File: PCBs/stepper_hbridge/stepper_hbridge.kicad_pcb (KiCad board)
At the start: 2 copper layers, 52.5 x 54.1 mm, 34 parts, among them J1 Conn_02x07_Odd_Even, J2 Conn_02x08_Odd_Even, J3 Conn_02x08_Odd_Even, J4 Conn_01x04_Pin, J5 Conn_01x04_Pin, J6 Conn_01x02_Pin, U1 L298N, U2 L298N, U3 NCP718xSN500

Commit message: both pcbs have smd capacitors, mounting holes, drc errors fixed
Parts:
- added H1: MountingHole, MountingHole:MountingHole_3.2mm_M3, F.Cu at (118.4, 55.7)
- added H2: MountingHole, MountingHole:MountingHole_3.2mm_M3, F.Cu at (162.2, 55.6)
- C2, C4: footprint Capacitor_THT:C_Radial_D8.0mm_H7.0mm_P3.50mm -> Capacitor_SMD:CP_Elec_6.3x7.7
- moved C4 5.44 mm to (119.7, 72.6), turned to 90 degrees
- moved C2 1.32 mm to (160.6, 77.2), turned to 90 degrees
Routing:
- net GND: track 30.9 -> 38.8 mm, vias 6 -> 8
- net +24V: track 172.9 -> 180.1 mm, vias 6 -> 7

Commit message: silkscreen
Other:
- board text added: "A B C D"
- board text added: "D4"
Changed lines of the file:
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@@
 		(tags "capacitor handsolder")
 		(property "Reference" "C6"
-			(at 0 -1.68 0)
+			(at 2.8425 0.17 0)
 			(layer "F.SilkS")
 			(effects
@@
 			(at 8.06 2.12 90)
 			(layer "F.SilkS")
+			(hide yes)
 			(effects
 				(font
@@
 		(tags "capacitor handsolder")
 		(property "Reference" "C9"
-			(at 0 -1.68 90)
+			(at 0.8175 1.82 90)
 			(layer "F.SilkS")
 			(effects
@@
 			(at 0 -4.35 90)
 			(layer "F.SilkS")
+			(hide yes)
 			(effects
 				(font
@@
 			(at 0.399 -1.601 90)
 			(layer "F.SilkS")
+			(hide yes)
 			(effects
 				(font
@@
 			(at 0 -2 90)
 			(layer "F.SilkS")
+			(hide yes)
 			(effects
 				(font
@@
 		(tags "capacitor handsolder")
 		(property "Reference" "C8"
-			(at 0 -1.68 90)
+			(at 1.3275 -1.68 90)
 			(layer "F.SilkS")
 			(effects
@@
 			(at 0 2 180)
 			(layer "B.SilkS")
+			(hide yes)
 			(effects
 				(font
@@
 			(at 0 3.9 0)
 			(layer "B.SilkS")
+			(hide yes)
 			(effects
 				(font
@@
 			(at 0 2 90)
 			(layer "B.SilkS")
+			(hide yes)
 			(effects
 				(font
@@
 			(at 0 2 0)
 			(layer "B.SilkS")
+			(hide yes)
 			(effects
 				(font
@@
 			(at 28.45 -9.49 0)
 			(layer "B.SilkS")
+			(hide yes)
 			(effects
 				(font
@@
 			(at 0 2 0)
 			(layer "B.SilkS")
+			(hide yes)
 			(effects
 				(font
@@
 		(tags "capacitor handsolder")
 		(property "Reference" "C7"
-			(at 0 1.68 0)
+			(at 0 -2.62 0)
 			(layer "B.SilkS")
 			(effects
@@
 			(at 0 2 0)
 			(layer "B.SilkS")
+			(hide yes)
 			(effects
 				(font
@@
 			(layer "B.Fab")
 		)
-		(fp_text user "${REFERENCE}"
-			(at 0 2 0)
-			(layer "B.Fab")
-			(effects
-				(font
-					(size 1 1)
-					(thickness 0.15)
-				)
-				(justify mirror)
-			)
-		)
 		(pad "1" smd roundrect
 			(at -1.65 0 180)
@@
 			(at 0 2 0)
 			(layer "B.SilkS")
+			(hide yes)
 			(effects
 				(font
@@
 		(layer "Edge.Cuts")
 	)
+	(gr_text "A B C D"
+		(at 127.97 104.02 0)
+		(layer "F.SilkS")
+		(effects
+			(font
+				(size 1 1)
+				(thickness 0.15)
+			)
+		)
+	)
+	(gr_text "A B C D"
+		(at 151.39 104.17 0)
+		(layer "F.SilkS")
+		(effects
+			(font
+				(size 1 1)
+				(thickness 0.15)
+			)
+		)
+	)
+	(gr_text "D4"
+		(at 126.48 110.98 0)
+		(layer "F.Fab")
+		(effects
+			(font
+				(size 1 1)
+				(thickness 0.15)
+			)
+		)
+	)
 	(gr_text_box "Ground Plane: Good (no extremely thin regions preventing overall continuity)\nDRC: 24V Power Header Capacitor Connection Error"

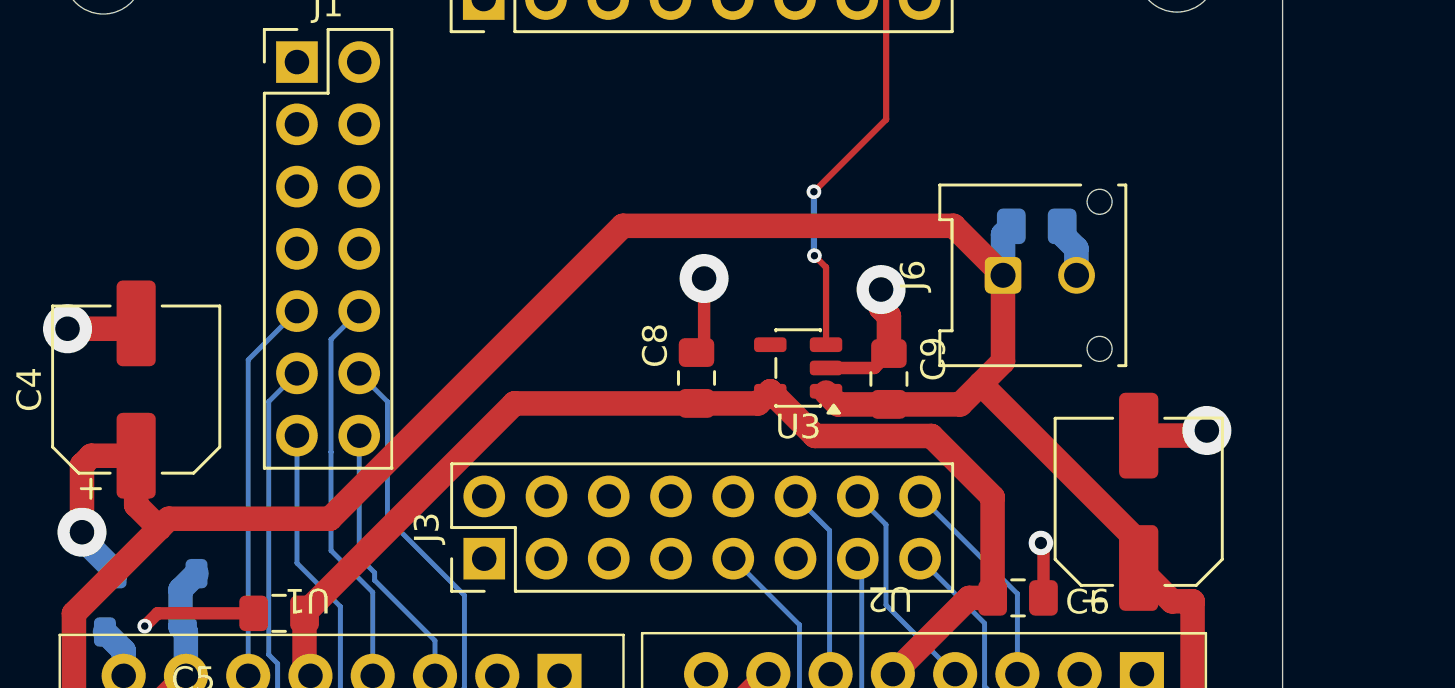
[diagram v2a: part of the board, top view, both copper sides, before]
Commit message: fixed 3.3V, fized header
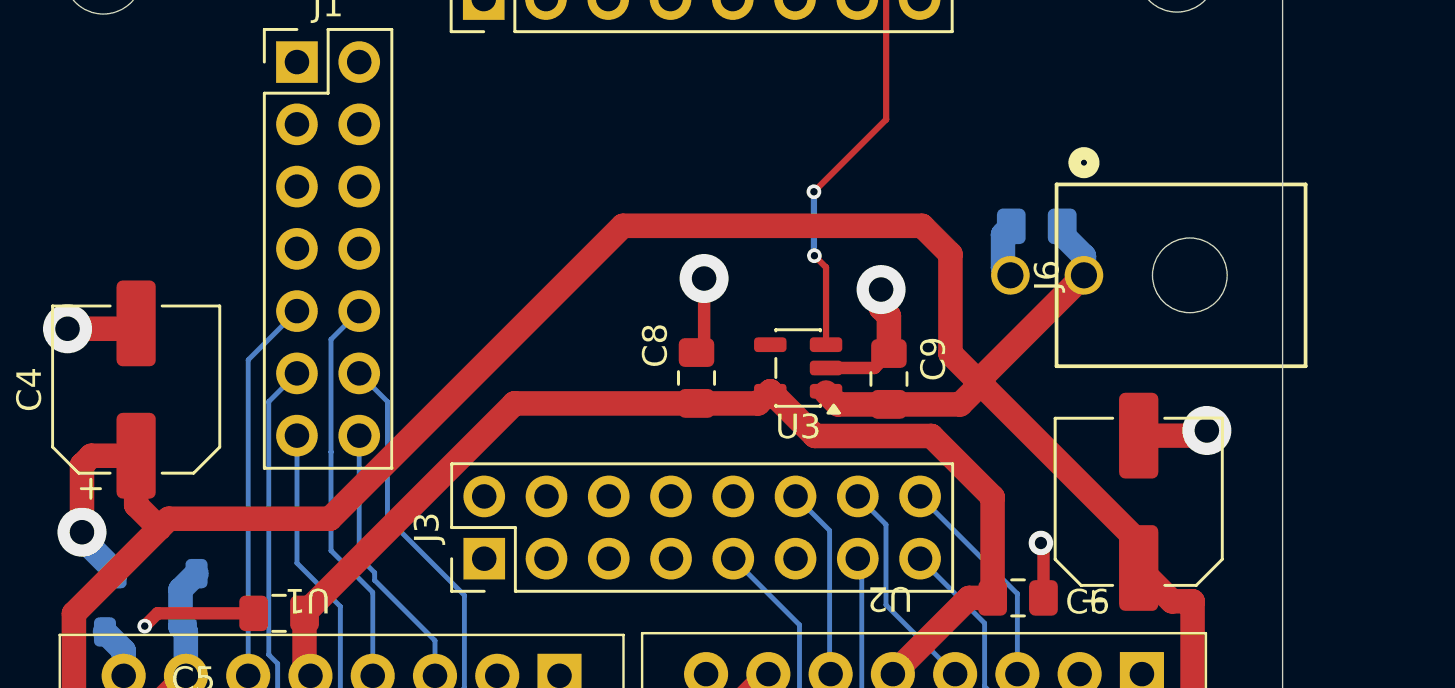
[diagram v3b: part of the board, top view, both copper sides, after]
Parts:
- J6: footprint Connector_Molex:Molex_Micro-Fit_3.0_43045-0212_2x01_P3.00mm_Vertical -> footprints:CONN_SD-43045-001_02_MOL
- moved J6 3.30 mm to (158.4, 67.9)
- turned C7 to 180 degrees
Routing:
- net +24V: track 180.1 -> 184.7 mm
